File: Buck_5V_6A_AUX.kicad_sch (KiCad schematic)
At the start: 13 parts, among them J22 AUX force-on, U5 TPSM63606RDLR

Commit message: Route the board and apply the prototype PCB checklist fixes
Routing
- Route power (pours, In2 power areas, vias) and all signals; add a
  Signal net class (0.15 mm width/clearance) for low-speed nets.
- J8 expansion header is now a 2x8 near the MCU.

Checklist red flags
- Crystal Y3 moved beside U1's OSC pins with C5/C6 outboard and no
  other signals under it.
- Vias untented by default (tented only under silkscreen); 15 mil
  test vias on key signals, recorded as DRC exclusions.
- ESD: U6/U7 split into four USBLC6-2SC6 (U6, U11, U7, U12), one per
  connector, with VBUS caps C50/C51; R12/R13 moved next to J13.
- GND test loop TP3 moved to the top edge beside J5.

Improvements
- Encoder connectors J7/J15 changed to keyed JST XH S4B side-entry.
- 43 passives/LEDs/FB2 moved from 0603 to 0805 (MPNs updated).
- Fifth M3 mounting hole H5 under J8.
- +3.3VA rerouted away from the crystal; acute track angles removed.
- Datasheet links filled in; silkscreen pin labels, pin maps, team
  names and date; reference labels cleared off pads and vias.
- Custom DRC rule for the J7/J15 silkscreen edge overhang.
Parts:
- C30: footprint Capacitor_SMD:C_0603_1608Metric -> Capacitor_SMD:C_0805_2012Metric; MPN GRM188R71C105KA12D -> GRM21BR71C105KA01L
- C31: footprint Capacitor_SMD:C_0603_1608Metric -> Capacitor_SMD:C_0805_2012Metric; MPN GRM1885C1H8R2DA01D -> C0805C829C5GACTU; Manufacturer Murata -> KEMET
- C40: footprint Capacitor_SMD:C_0603_1608Metric -> Capacitor_SMD:C_0805_2012Metric; MPN GRM1885C1H102JA01D -> C0805C102J5GACTU; Manufacturer Murata -> KEMET
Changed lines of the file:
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@@
 			)
 		)
-		(property "Footprint" "Capacitor_SMD:C_0603_1608Metric"
-			(at 68.58 107.95 0)
-			(hide yes)
-			(show_name no)
-			(do_not_autoplace no)
-			(effects
-				(font
-					(size 1.27 1.27)
-				)
-			)
-		)
-		(property "Datasheet" "~"
+		(property "Footprint" "Capacitor_SMD:C_0805_2012Metric"
+			(at 68.58 107.95 0)
+			(hide yes)
+			(show_name no)
+			(do_not_autoplace no)
+			(effects
+				(font
+					(size 1.27 1.27)
+				)
+			)
+		)
+		(property "Datasheet" "https://content.kemet.com/datasheets/KEM_C1003_C0G_SMD.pdf"
 			(at 68.58 107.95 0)
 			(hide yes)
@@
 			)
 		)
-		(property "Manufacturer" "Murata"
-			(at 68.58 107.95 0)
-			(hide yes)
-			(show_name no)
-			(do_not_autoplace no)
-			(effects
-				(font
-					(size 1.27 1.27)
-				)
-			)
-		)
-		(property "MPN" "GRM1885C1H102JA01D"
+		(property "Manufacturer" "KEMET"
+			(at 68.58 107.95 0)
+			(hide yes)
+			(show_name no)
+			(do_not_autoplace no)
+			(effects
+				(font
+					(size 1.27 1.27)
+				)
+			)
+		)
+		(property "MPN" "C0805C102J5GACTU"
 			(at 68.58 107.95 0)
 			(hide yes)
@@
 			)
 		)
-		(property "Footprint" "Capacitor_SMD:C_0603_1608Metric"
+		(property "Footprint" "Capacitor_SMD:C_0805_2012Metric"
 			(at 194.01 96.52 0)
 			(hide yes)
@@
 			)
 		)
-		(property "Datasheet" "https://search.murata.co.jp/Ceramy/image/img/A01X/G101/ENG/GRM1885C1H8R2DA01-01A.pdf"
+		(property "Datasheet" "https://content.kemet.com/datasheets/KEM_C1003_C0G_SMD.pdf"
 			(at 193.04 92.71 0)
 			(hide yes)
@@
 			)
 		)
-		(property "Manufacturer" "Murata"
-			(at 193.04 92.71 0)
-			(hide yes)
-			(show_name no)
-			(do_not_autoplace no)
-			(effects
-				(font
-					(size 1.27 1.27)
-				)
-			)
-		)
-		(property "MPN" "GRM1885C1H8R2DA01D"
+		(property "Manufacturer" "KEMET"
+			(at 193.04 92.71 0)
+			(hide yes)
+			(show_name no)
+			(do_not_autoplace no)
+			(effects
+				(font
+					(size 1.27 1.27)
+				)
+			)
+		)
+		(property "MPN" "C0805C829C5GACTU"
 			(at 193.04 92.71 0)
 			(hide yes)
@@
 			)
 		)
-		(property "Footprint" "Capacitor_SMD:C_0603_1608Metric"
+		(property "Footprint" "Capacitor_SMD:C_0805_2012Metric"
 			(at 103.84 114.3 0)
 			(hide yes)
@@
 			)
 		)
-		(property "Datasheet" "https://search.murata.co.jp/Ceramy/image/img/A01X/G101/ENG/GRM188R71C105KA12-01.pdf"
+		(property "Datasheet" "https://www.murata.com/en-us/products/productdetail?partno=GRM21BR71C105KA01%23"
 			(at 102.87 110.49 0)
 			(hide yes)
@@
 			)
 		)
-		(property "MPN" "GRM188R71C105KA12D"
-			(at 102.87 110.49 0)
-			(hide yes)
+		(property "MPN" "GRM21BR71C105KA01L"
+			(at 102.87 110.49 0)
+			(hide yes)

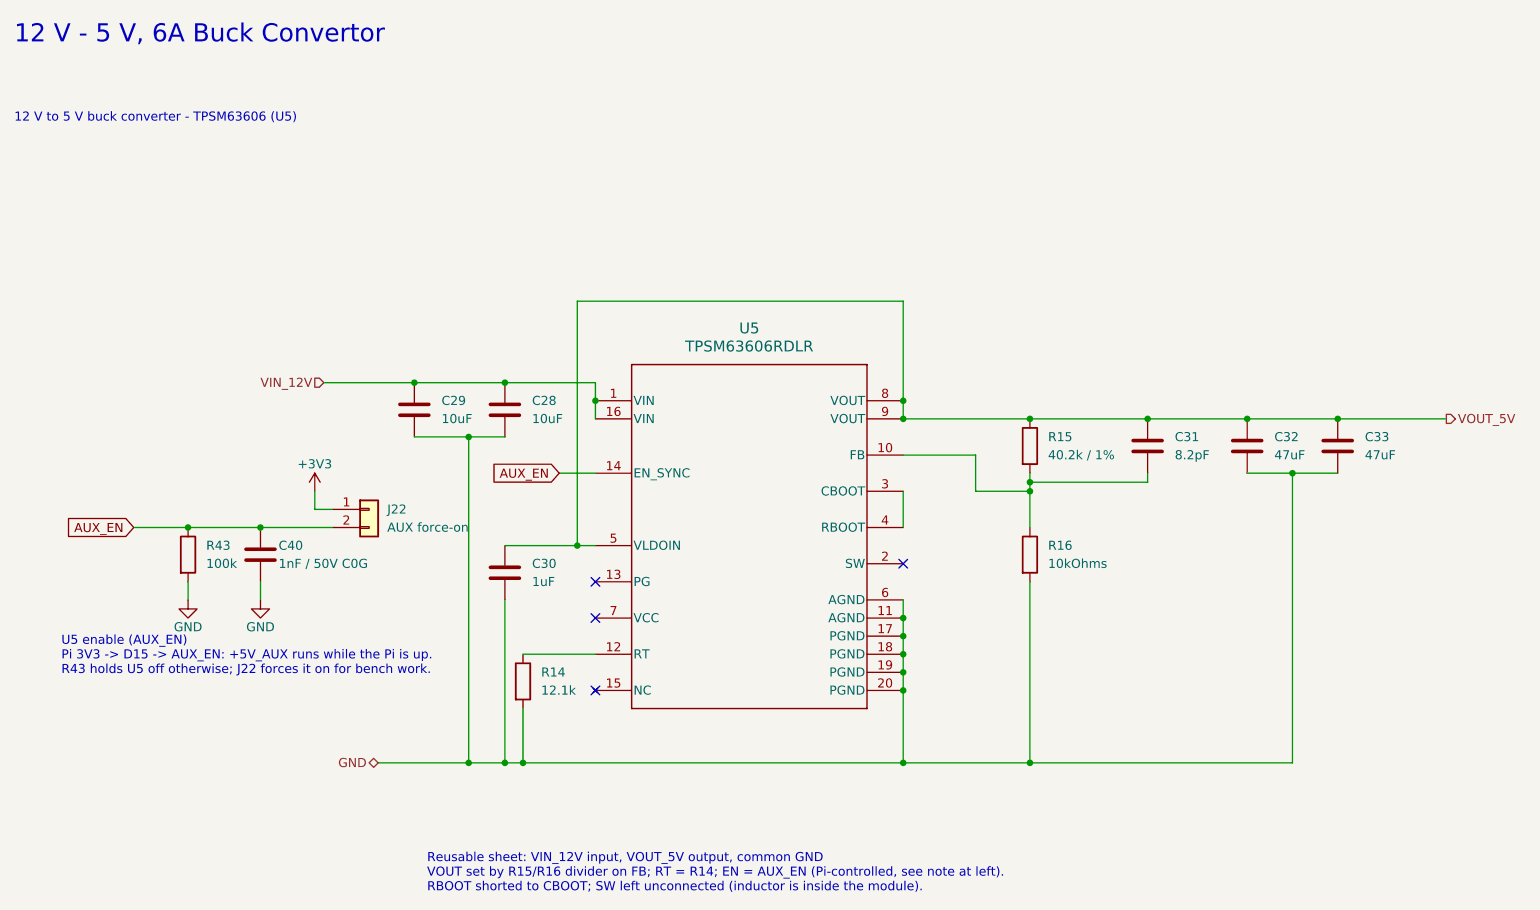
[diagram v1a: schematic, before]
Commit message: Replace out-of-stock buck converters with in-stock TI parts
TPSM63606 (U2, U5) and TPS54202 (U3) are out of stock at DigiKey.

- U2 (Pi 5 V) and U5 (AUX 5 V), 6 A: TPS56637RPAR with Wurth
  74439387033 3.3 uH, 2x 10 uF + 100 nF in, 47 uF out, 73.2k/10k
  feedback with 20k + 100 pF feed-forward, 100k PG pull-up. Values
  from TI WEBENCH (10-15 V in, 5 V 6 A); load-step sim 0.6->6 A
  stays within 4.91-5.06 V.
- U3 (+5V_SYS), 2 A: TPS54202HDDCR with TDK VLS6045EX-100M 10 uH,
  22 uF in, 47 uF out, 100k/13.7k + 68 pF, and a new 442k EN pull-up
  (R63) since the H version's EN is pulled down internally. Load-step
  sim 0.2->2 A stays within 4.72-5.21 V.
- New TPS56637 symbol, RPA0010A footprint (TI land pattern) and
  WE-XHMI-7070 footprint (Wurth land pattern).
- Layout follows the datasheet layout examples: TPS56637 Figure 34
  (VIN/Cin, inductor/Cout, AGND island, via arrays, inner-layer
  mirrors) and TPS54202H Figure 10-1 (SW through vias on an inner
  pour to the inductor, caps between GND and VIN copper).
- U5 moved below J8; PB7, PI_BOOT0, USART2_RX and the +5V_SYS feed
  rerouted around the new parts. New PG/EN resistors are R61-R63 to
  avoid the refs used on feat/battery-monitor-interior-light.
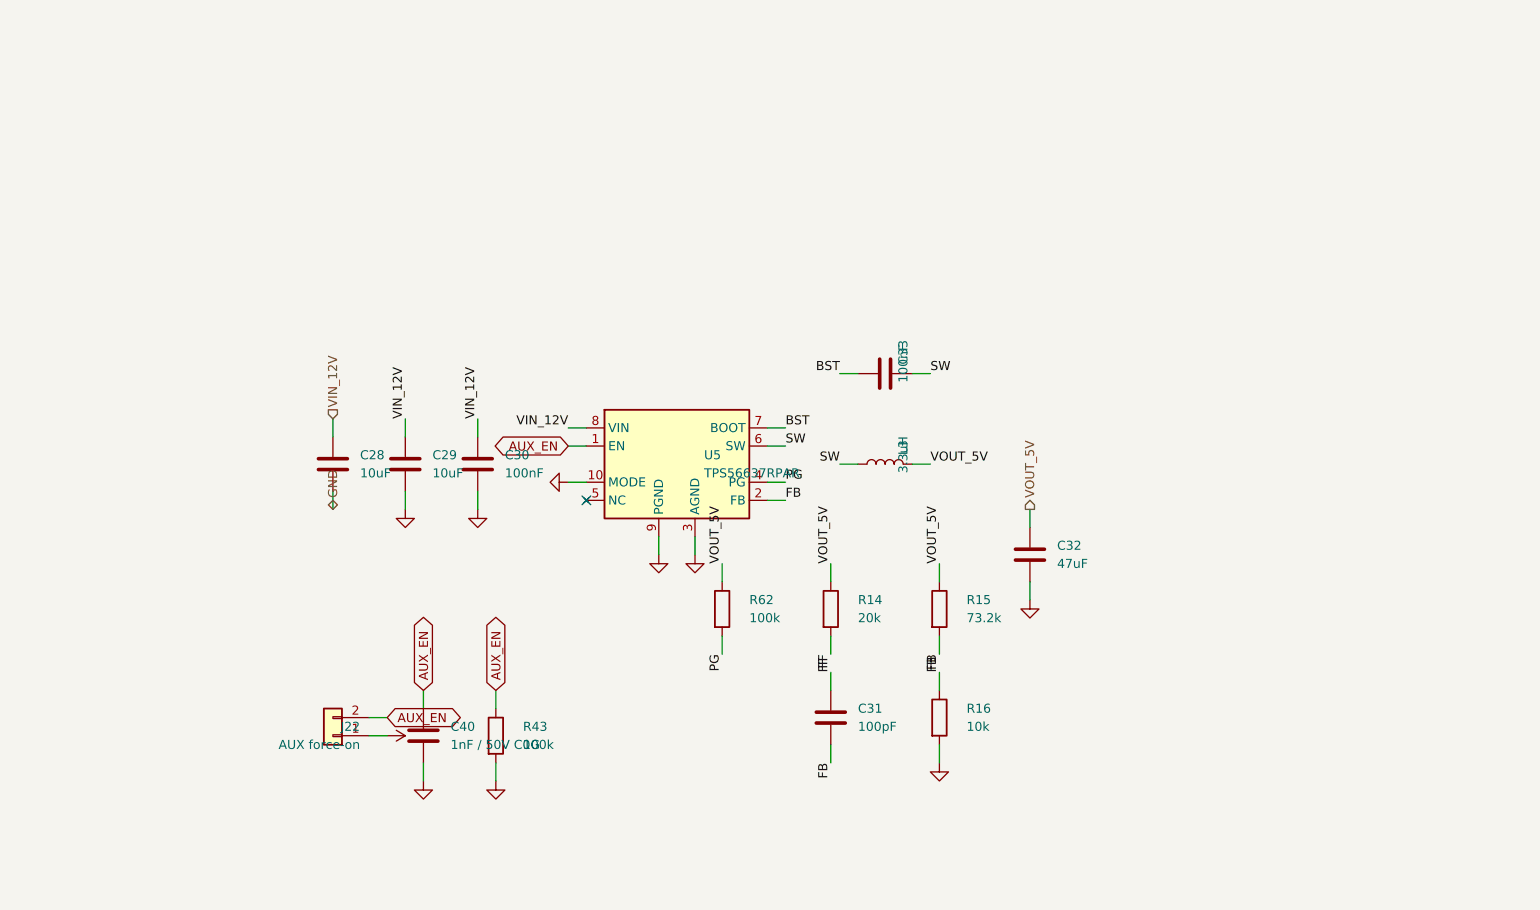
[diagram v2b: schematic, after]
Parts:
- added L3: 3.3uH, project_footprints:L_Wuerth_WE-XHMI-7070, symbol Device:L
- added R62: 100k, Resistor_SMD:R_0805_2012Metric, symbol Device:R
- C28, C29: footprint Capacitor_SMD:C_1210_3225Metric -> Capacitor_SMD:C_1206_3216Metric; MPN GRM32ER71H106KA12L -> GRM31CR71E106KA12L; Specification 10uF / 50V X7R -> 10uF / 25V X7R 1206 (Cin)
- C30: value 1uF -> 100nF; MPN GRM21BR71C105KA01L -> C0805C104K5RACTU; Manufacturer Murata -> KEMET; Specification 1uF / 16V X7R -> 100nF / 50V X7R (Cinx)
- C31: value 8.2pF -> 100pF; MPN C0805C829C5GACTU -> C0805C101J5GACTU; Specification 8.2pF / 50V C0G -> 100pF / 50V C0G (Cff)
- C32: footprint project_footprints:C_Murata_GRM32ER71A476ME15 -> Capacitor_SMD:C_1210_3225Metric; MPN GRM32ER71A476ME15L -> GRM32ER61C476KE15L; Specification 47uF / 10V X7R -> 47uF / 16V X5R 1210 (Cout)
- C33: value 47uF -> 100nF; footprint project_footprints:C_Murata_GRM32ER71A476ME15 -> Capacitor_SMD:C_0805_2012Metric; MPN GRM32ER71A476ME15L -> C0805C104K5RACTU; Manufacturer Murata -> KEMET; Specification 47uF / 10V X7R -> 100nF / 50V X7R (Cboot)
- R14: value 12.1k -> 20k; MPN (none) -> ERJ-6ENF2002V; Manufacturer (none) -> Panasonic; Specification (none) -> 20k 1% (Rff)
- R15: value 40.2k / 1% -> 73.2k; MPN (none) -> RC0805FR-0773K2L; Manufacturer (none) -> Yageo; Specification (none) -> 73.2k 1% (Rfbt)
- R16: value 10kOhms -> 10k; MPN (none) -> RC0805FR-0710KL; Manufacturer (none) -> Yageo; Specification (none) -> 10k 1% (Rfbb)
- U5: value TPSM63606RDLR -> TPS56637RPAR; footprint project_footprints:RDL0020A-MFG -> project_footprints:TI_RPA0010A_VQFN-HR-10_3x3mm; symbol TPSM63606RDLR:PTPSM63606RDLR -> TPS56637RPAR:TPS56637RPAR; Design Notes VOUT = VREF x (1 + R15/R16) with FB divider R15 40.2k / R16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 -> (none); Key Specs VIN 3-36 V; VOUT 1-16 V adjustable; IOUT max 6 A; fsw 200 k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 -> (none); MPN TPSM63606RDLR -> TPS56637RPAR; Product Page https://www.ti.com/product/TPSM63606 -> (none); Specification (none) -> 6 A buck, 557 kHz, MODE=GND (Eco-mode); Used In Sheet Buck_5V_6A_AUX: 12 V in, +5V_AUX net out -> (none)
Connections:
- net AUX_EN: now also U5.1 (EN); no longer U5.14 (EN_SYNC)
- net GND: now also U5.10 (MODE), U5.3 (AGND), U5.9 (PGND); no longer C33.2, R14.2, U5.11 (AGND), U5.17 (PGND), U5.18 (PGND), U5.19 (PGND), U5.20 (PGND), U5.6 (AGND)
- net VIN_12V: now also C30.1, U5.8 (VIN); no longer U5.1 (VIN), U5.16 (VIN)
- net VOUT_5V: now also R14.1, L3.2, R62.1; no longer C30.1, C31.1, C33.1, U5.5 (VLDOIN), U5.8 (VOUT), U5.9 (VOUT)
- net FB: now reaches C31.2, R15.2, R16.1
- net FB: now also U5.2 (FB); no longer U5.10 (FB)
- net PG: now reaches U5.4 (PG)
- net PG: now also R62.2; no longer U5.3 (CBOOT)
- net BST: now reaches U5.7 (BOOT)
- net BST: now also C33.1
- new net FF: C31.1, R14.2
- new net SW: C33.2, L3.1, U5.6 (SW)
- no-connect marks 4 -> 1
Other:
- note removed: "12 V - 5 V, 6A Buck Convertor"
- note removed: "12 V to 5 V buck converter - TPSM63606 (U5)"
- note removed: "Reusable sheet: VIN_12V input, VOUT_5V output, common GND VOUT set by R15/R16 divider on FB; RT = R14; EN = AUX_EN (Pi-controlled, see note at left). RBOOT shorted to CBOOT; SW left unconnected (inductor is inside the module)."
- note removed: "U5 enable (AUX_EN) Pi 3V3 -> D15 -> AUX_EN: +5V_AUX runs while the Pi is up. R43 holds U5 off otherwise; J22 forces it on for bench work."
- moved on the sheet: C28, C29, C30, C31, C32, C33, C40, J22, R14, R15, R16, R43
